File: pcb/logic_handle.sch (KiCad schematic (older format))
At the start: 52 parts, among them J1 Conn_01x05_Male, Q1 BSS214NW, SW1 SW_Push, U1 NCP1117-3.3_TO252, U2 TXS0108EPW, U3 MSP430FR5739IDAR, Y1 Crystal

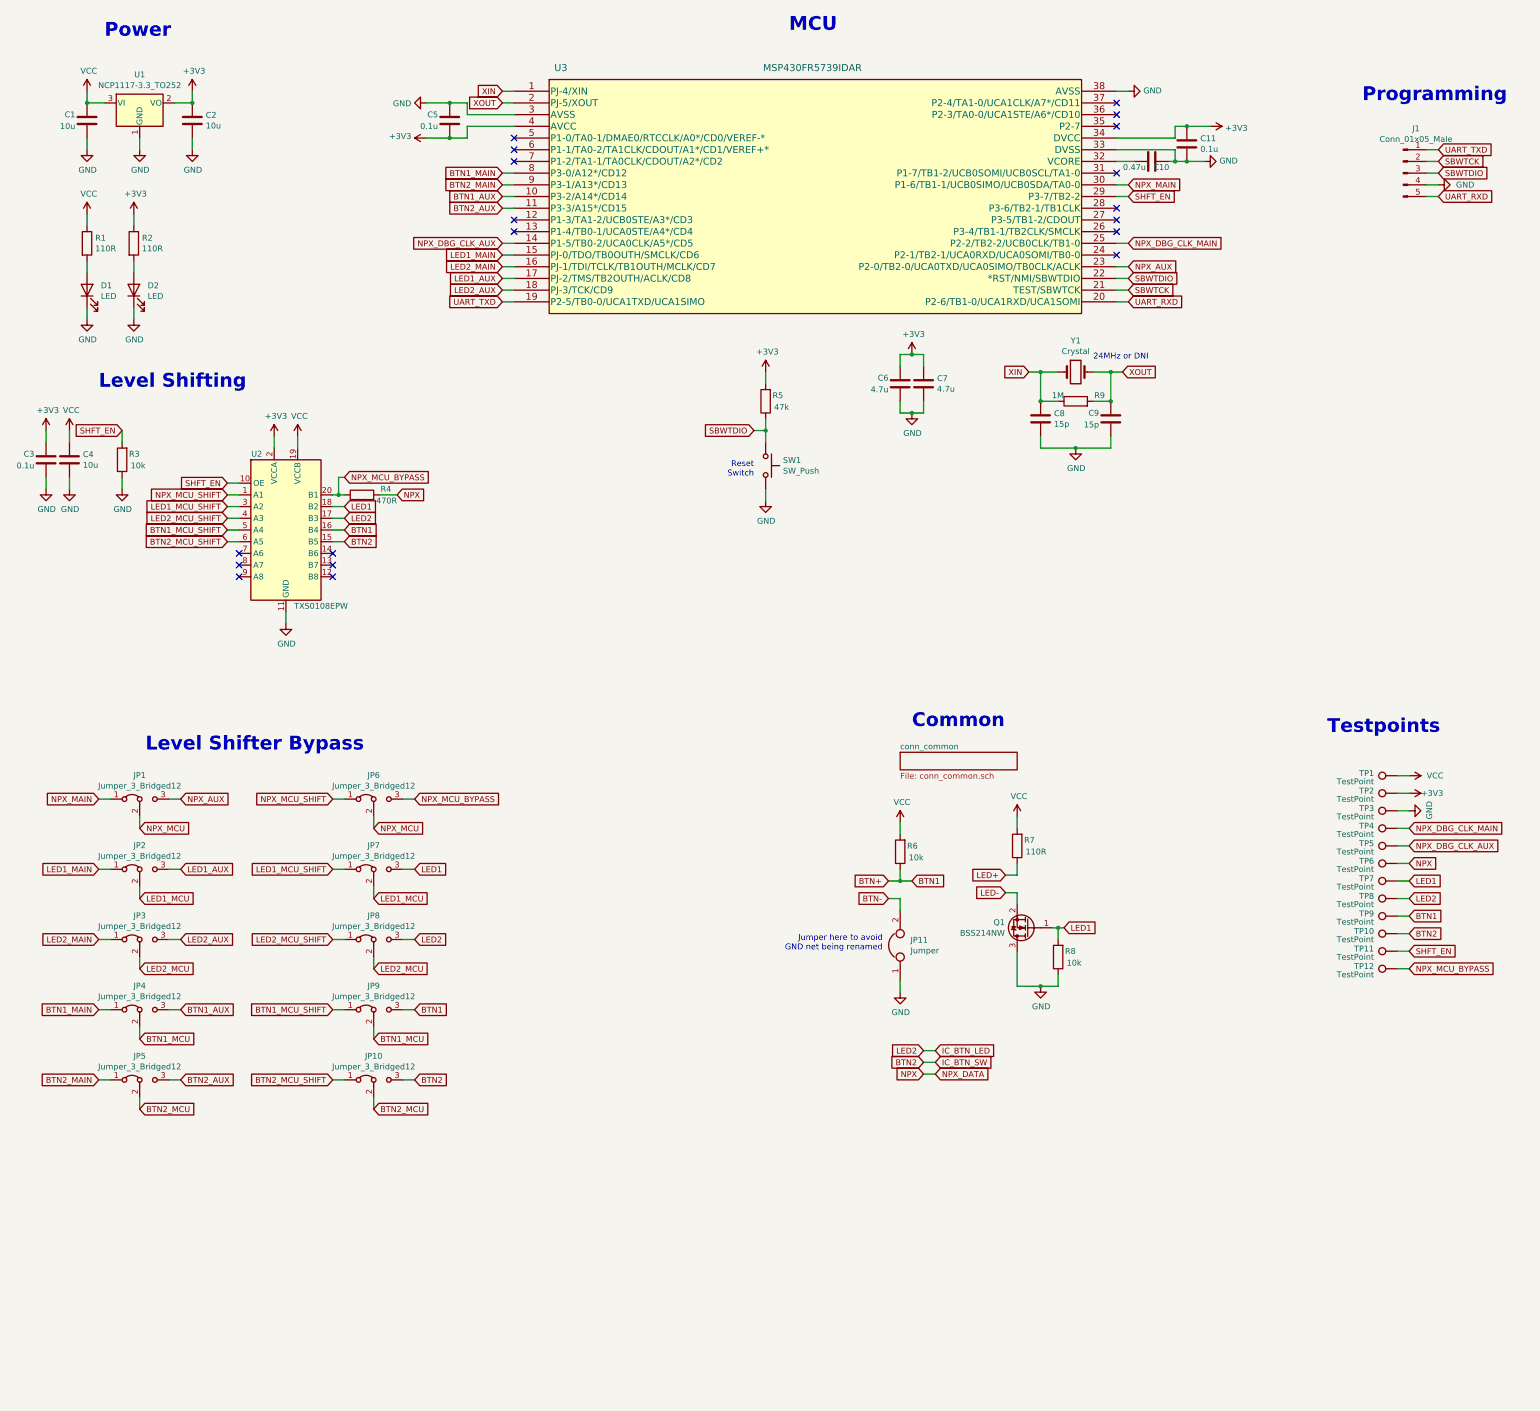
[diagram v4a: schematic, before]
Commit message: pcb: implement improvements described in rev 1 bringup notes (#23)
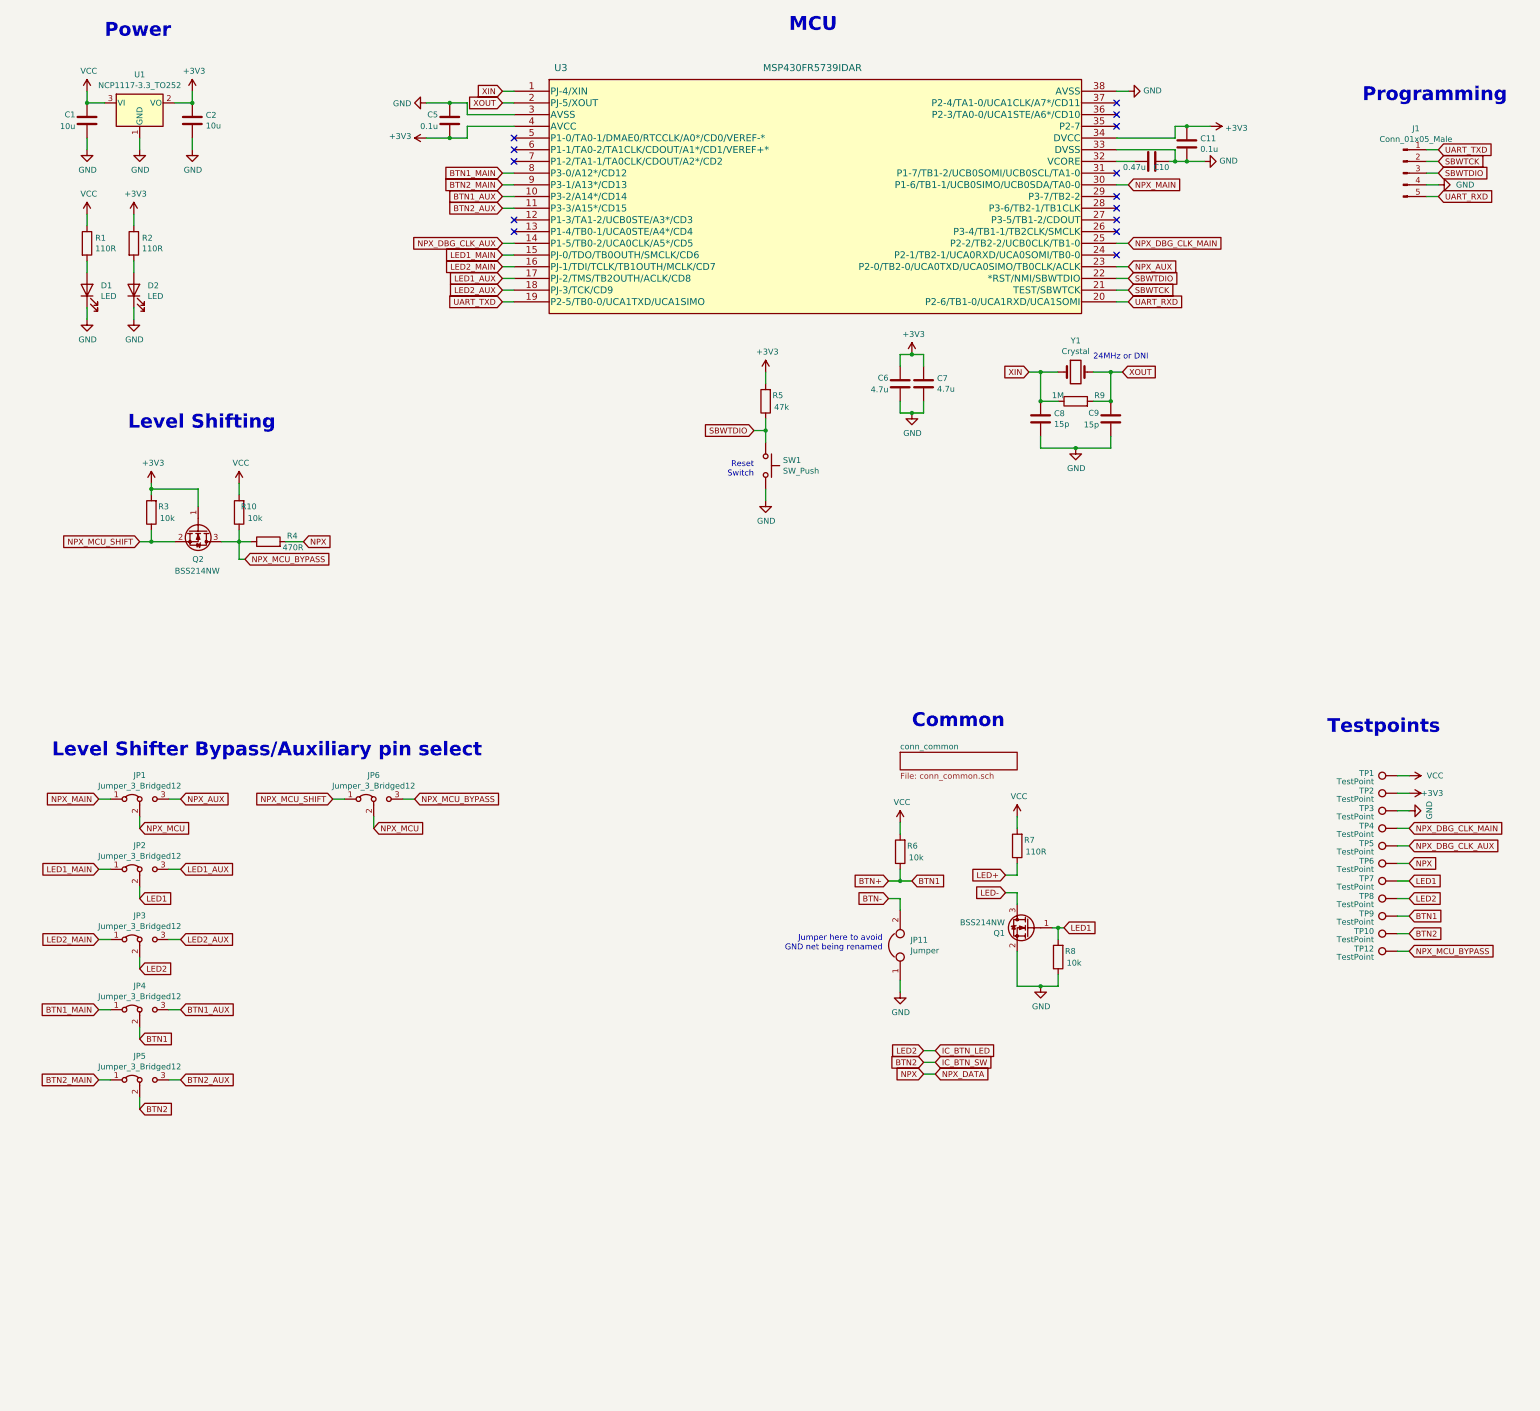
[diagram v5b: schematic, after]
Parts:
- removed C3: 0.1u, Capacitor_SMD:C_0805_2012Metric, symbol Device:C
- removed C4: 10u, Capacitor_SMD:C_0805_2012Metric, symbol Device:C
- removed JP10, JP7, JP8, JP9: Jumper_3_Bridged12, Jumper:SolderJumper-3_P1.3mm_Bridged2Bar12_Pad1.0x1.5mm, symbol Jumper:Jumper_3_Bridged12
- removed TP11: TestPoint, TestPoint:TestPoint_Pad_2.0x2.0mm, symbol Connector:TestPoint
- removed U2: TXS0108EPW, Package_SO:TSSOP-20_4.4x6.5mm_P0.65mm, symbol Logic_LevelTranslator:TXS0108EPW
- added Q2: BSS214NW, Package_TO_SOT_SMD:SOT-323_SC-70, symbol Transistor_FET:BSS214NW
- added R10: 10k, Resistor_SMD:R_0805_2012Metric, symbol Device:R
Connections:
- net BTN1_MCU is gone; now on net BTN+: JP4.2 (C)
- net BTN2_MCU is gone; now on net BTN2: JP5.2 (C)
- net LED1_MCU is gone; now on net LED1: JP2.2 (C)
- net LED2_MCU is gone; now on net IC_BTN_LED: JP3.2 (C)
- net +3V3: now also R3.2, Q2.1 (G)
- net GND: now also Q1.2 (S); no longer Q1.3 (D), R3.1
- net LED-: now also Q1.3 (D); no longer Q1.2 (S)
- net NPX_MCU_BYPASS: now also Q2.3 (D), R10.1
- net NPX_MCU_SHIFT: now also R3.1, Q2.2 (S)
- net VCC: now also R10.2
- net SHFT_EN: no longer names the net of U3.29 (P3-7/TB2-2)
- net SHFT_EN: no longer R3.2
- no-connect marks 19 -> 14
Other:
- note added: "Level Shifter Bypass/Auxiliary pin select"
- note removed: "Level Shifter Bypass"
- moved on the sheet: R4, TP12

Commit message: Revert "pcb: implement improvements described in rev 1 bringup notes (#23)"
This reverts commit 01e55846632a9cef383a24172751afed95ee1909.
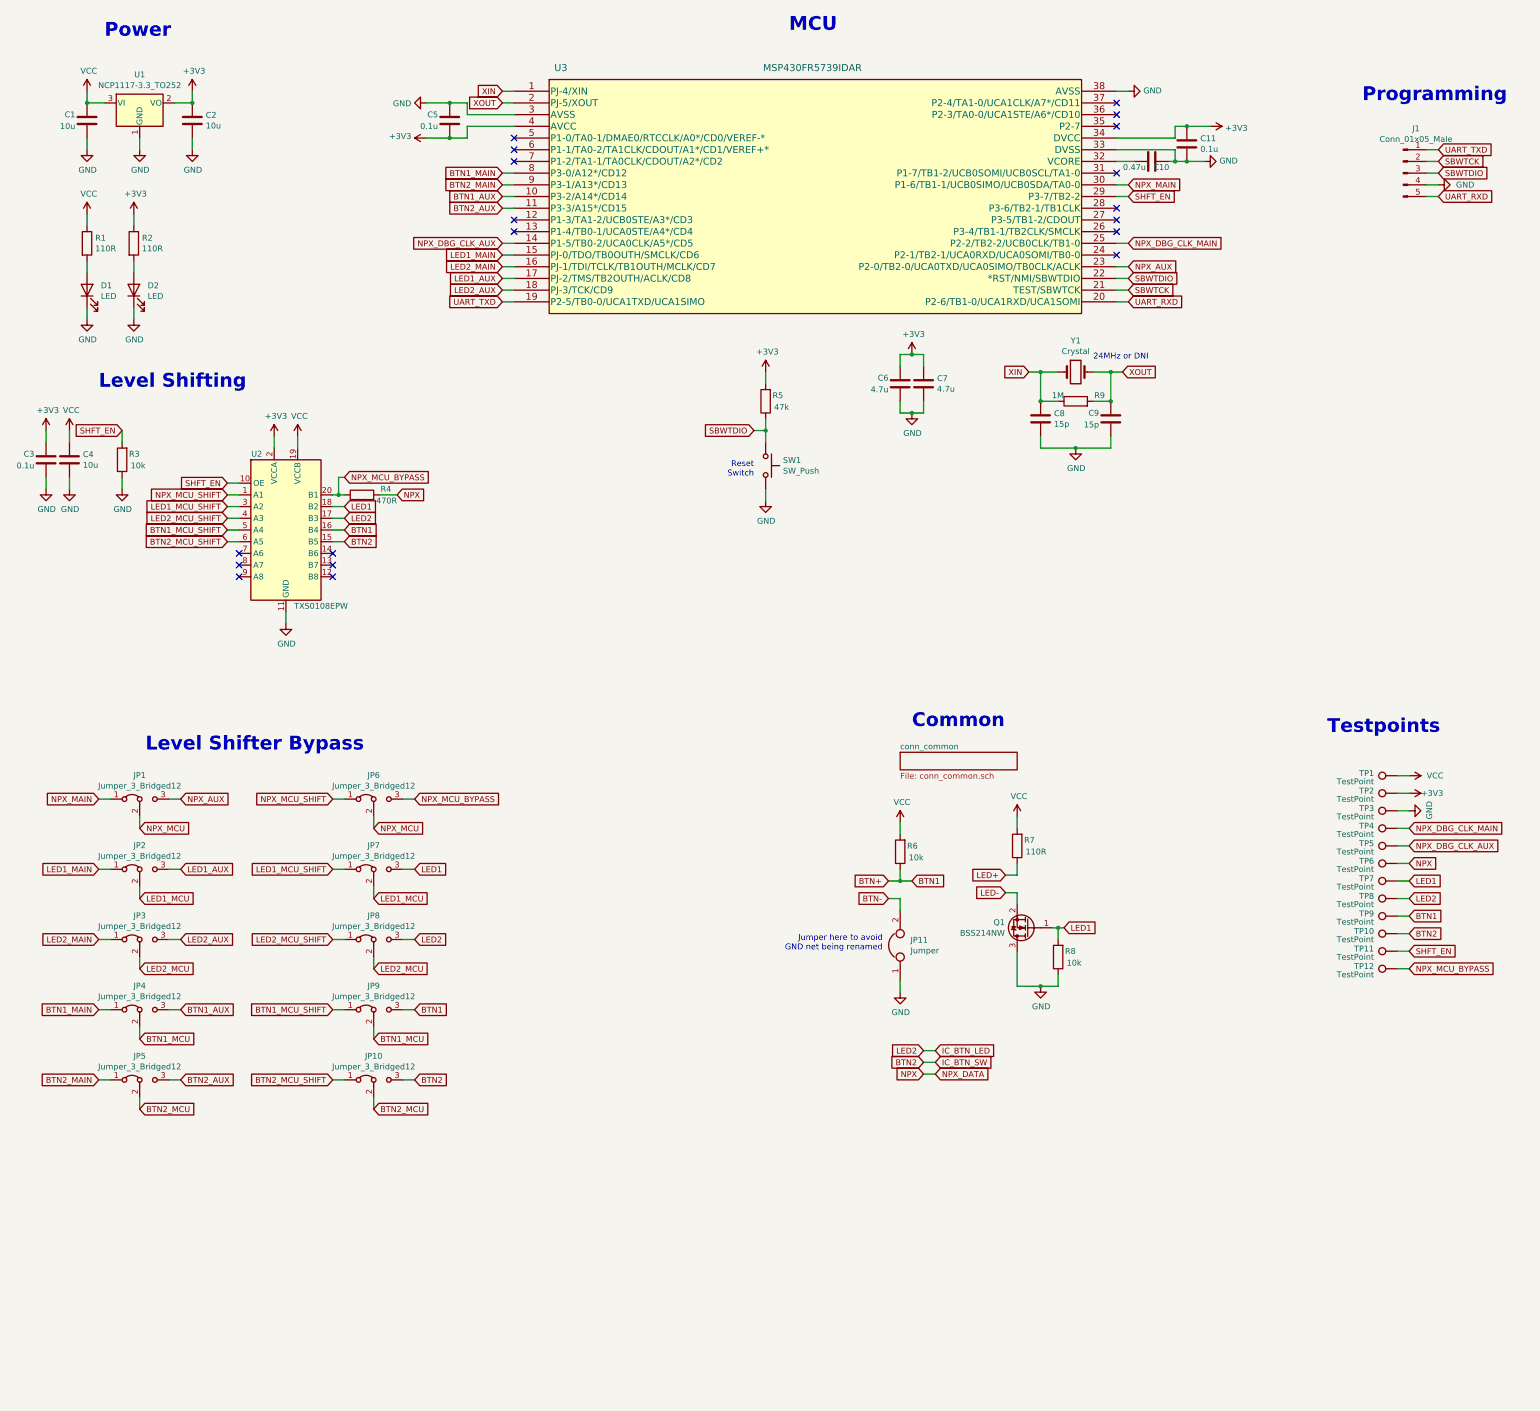
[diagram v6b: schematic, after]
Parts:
- removed Q2: BSS214NW, Package_TO_SOT_SMD:SOT-323_SC-70, symbol Transistor_FET:BSS214NW
- removed R10: 10k, Resistor_SMD:R_0805_2012Metric, symbol Device:R
- added C3: 0.1u, Capacitor_SMD:C_0805_2012Metric, symbol Device:C
- added C4: 10u, Capacitor_SMD:C_0805_2012Metric, symbol Device:C
- added JP10, JP7, JP8, JP9: Jumper_3_Bridged12, Jumper:SolderJumper-3_P1.3mm_Bridged2Bar12_Pad1.0x1.5mm, symbol Jumper:Jumper_3_Bridged12
- added TP11: TestPoint, TestPoint:TestPoint_Pad_2.0x2.0mm, symbol Connector:TestPoint
- added U2: TXS0108EPW, Package_SO:TSSOP-20_4.4x6.5mm_P0.65mm, symbol Logic_LevelTranslator:TXS0108EPW
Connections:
- net +3V3: now also C3.2, U2.2 (VCCA); no longer R3.2
- net BTN+: now also JP9.3 (B), U2.16 (B4); no longer JP4.2 (C)
- net BTN2: now also JP10.3 (B), U2.15 (B5); no longer JP5.2 (C)
- net GND: now also Q1.3 (D), R3.1, C3.1, C4.2, U2.11 (GND); no longer Q1.2 (S)
- net IC_BTN_LED: now also JP8.3 (B), U2.17 (B3); no longer JP3.2 (C)
- net LED-: now also Q1.2 (S); no longer Q1.3 (D)
- net LED1: now also JP7.3 (B), U2.18 (B2); no longer JP2.2 (C)
- net NPX_MCU_BYPASS: now also U2.20 (B1)
- net NPX_MCU_SHIFT: now also U2.1 (A1); no longer R3.1
- net VCC: now also C4.1, U2.19 (VCCB)
- net SHFT_EN: now reaches U3.29 (P3-7/TB2-2)
- net SHFT_EN: now also R3.2, TP11.1, U2.10 (OE)
- new net BTN1_MCU: JP4.2 (C), JP9.2 (C)
- new net BTN1_MCU_SHIFT: JP9.1 (A), U2.5 (A4)
- new net BTN2_MCU: JP10.2 (C), JP5.2 (C)
- new net BTN2_MCU_SHIFT: JP10.1 (A), U2.6 (A5)
- new net LED1_MCU: JP2.2 (C), JP7.2 (C)
- new net LED1_MCU_SHIFT: JP7.1 (A), U2.3 (A2)
- new net LED2_MCU: JP3.2 (C), JP8.2 (C)
- new net LED2_MCU_SHIFT: JP8.1 (A), U2.4 (A3)
- no-connect marks 14 -> 19
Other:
- note added: "Level Shifter Bypass"
- note removed: "Level Shifter Bypass/Auxiliary pin select"
- moved on the sheet: R4, TP12
